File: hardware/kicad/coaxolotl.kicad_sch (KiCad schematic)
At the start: 0 parts

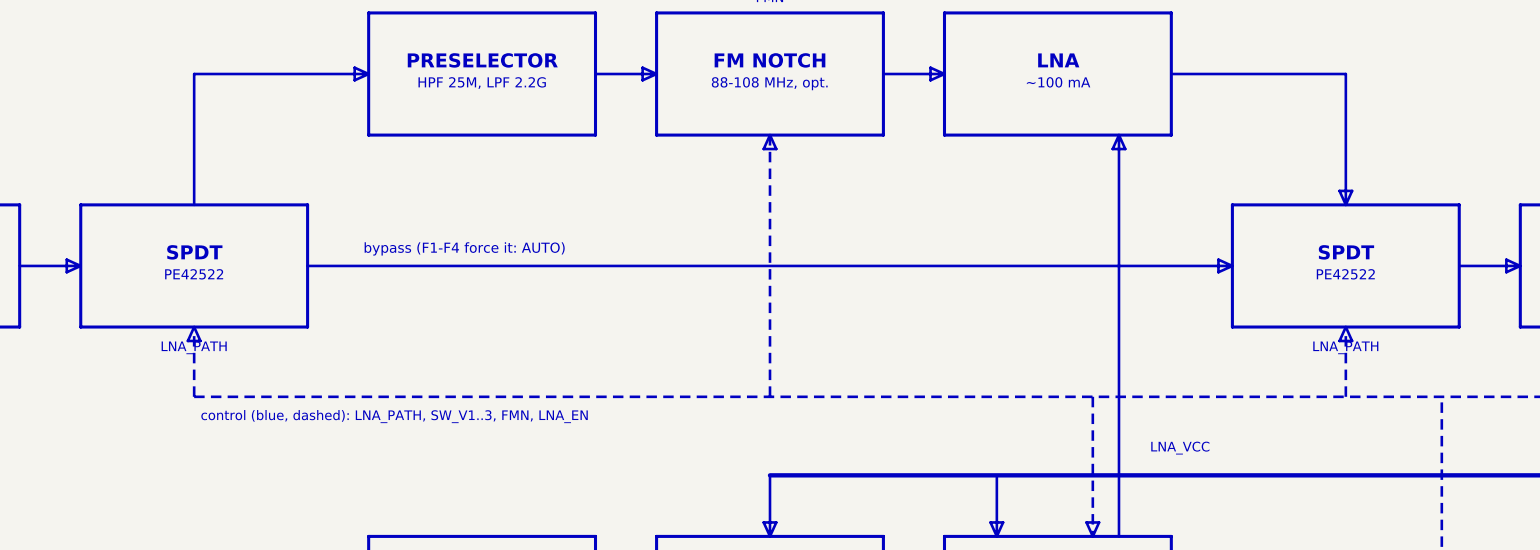
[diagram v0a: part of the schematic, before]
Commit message: Schematic: PE42520 SPDTs instead of PE42522
PE42520C-Z (QFN-16 3x3, LCSC C500478) pinout and truth table checked
against the LCSC datasheet: LS tied to VDD so CTRL = 0 selects RF1
(bypass) and the firmware stays unchanged. KiCad library footprint
QFN-16-1EP_3x3mm_P0.5mm_EP1.7x1.7mm.

Co-Authored-By: Claude Opus 5.5 <noreply@anthropic.com>
Claude-Session: https://claude.ai/code/session_01YRUiF8Vp4242sya9Xyg3TV
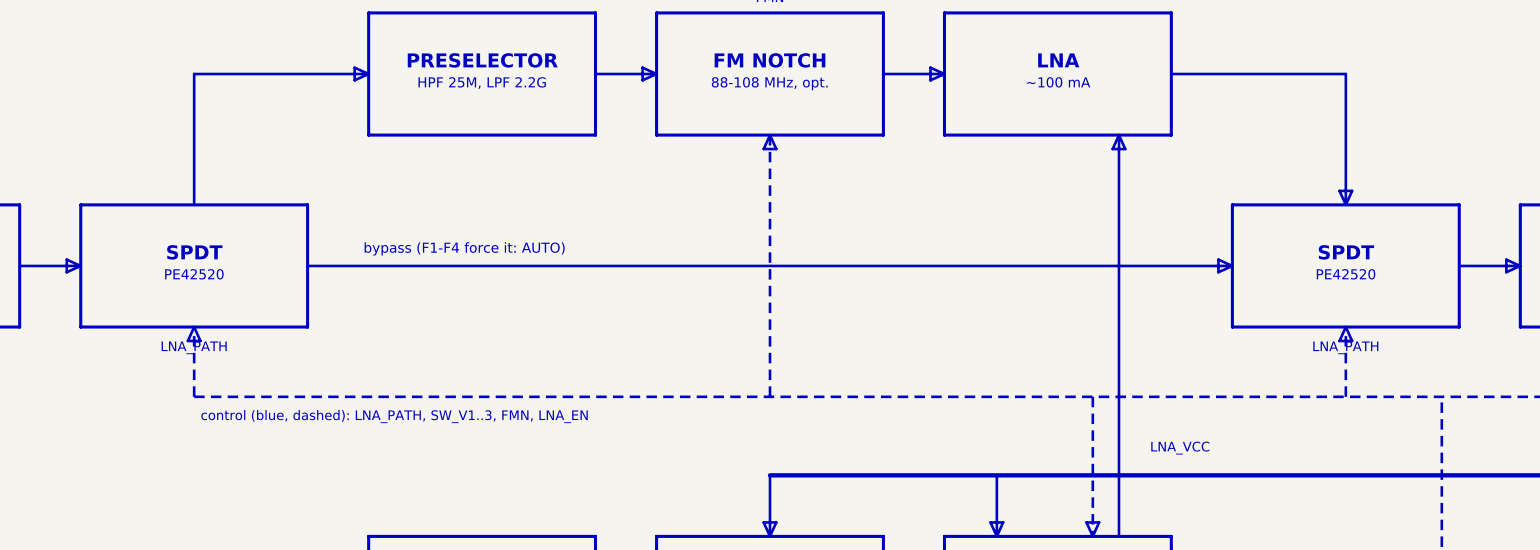
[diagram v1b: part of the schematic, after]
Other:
- note added: "PE42520"
- note removed: "PE42522"
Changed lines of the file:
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@@
     )
   )
-  (text "PE42522"
+  (text "PE42520"
     (at 97 68.25 0)
     (effects
@@
     )
   )
-  (text "PE42522"
+  (text "PE42520"
     (at 229 68.25 0)
     (effects
@@
     (instances
       (project "coaxolotl"
-        (path "/aac636a4-9bcf-4dd9-bf59-957fc0b2357f"
+        (path "/1b55bade-2730-4b67-9af5-55f72c383bca"
           (page "2")
         )
@@
     (instances
       (project "coaxolotl"
-        (path "/aac636a4-9bcf-4dd9-bf59-957fc0b2357f"
+        (path "/1b55bade-2730-4b67-9af5-55f72c383bca"
           (page "3")
         )
@@
     (instances
       (project "coaxolotl"
-        (path "/aac636a4-9bcf-4dd9-bf59-957fc0b2357f"
+        (path "/1b55bade-2730-4b67-9af5-55f72c383bca"
           (page "4")
         )
@@
     (instances
       (project "coaxolotl"
-        (path "/aac636a4-9bcf-4dd9-bf59-957fc0b2357f"
+        (path "/1b55bade-2730-4b67-9af5-55f72c383bca"
           (page "5")
         )
@@
     (instances
       (project "coaxolotl"
-        (path "/aac636a4-9bcf-4dd9-bf59-957fc0b2357f"
+        (path "/1b55bade-2730-4b67-9af5-55f72c383bca"
           (page "6")
         )

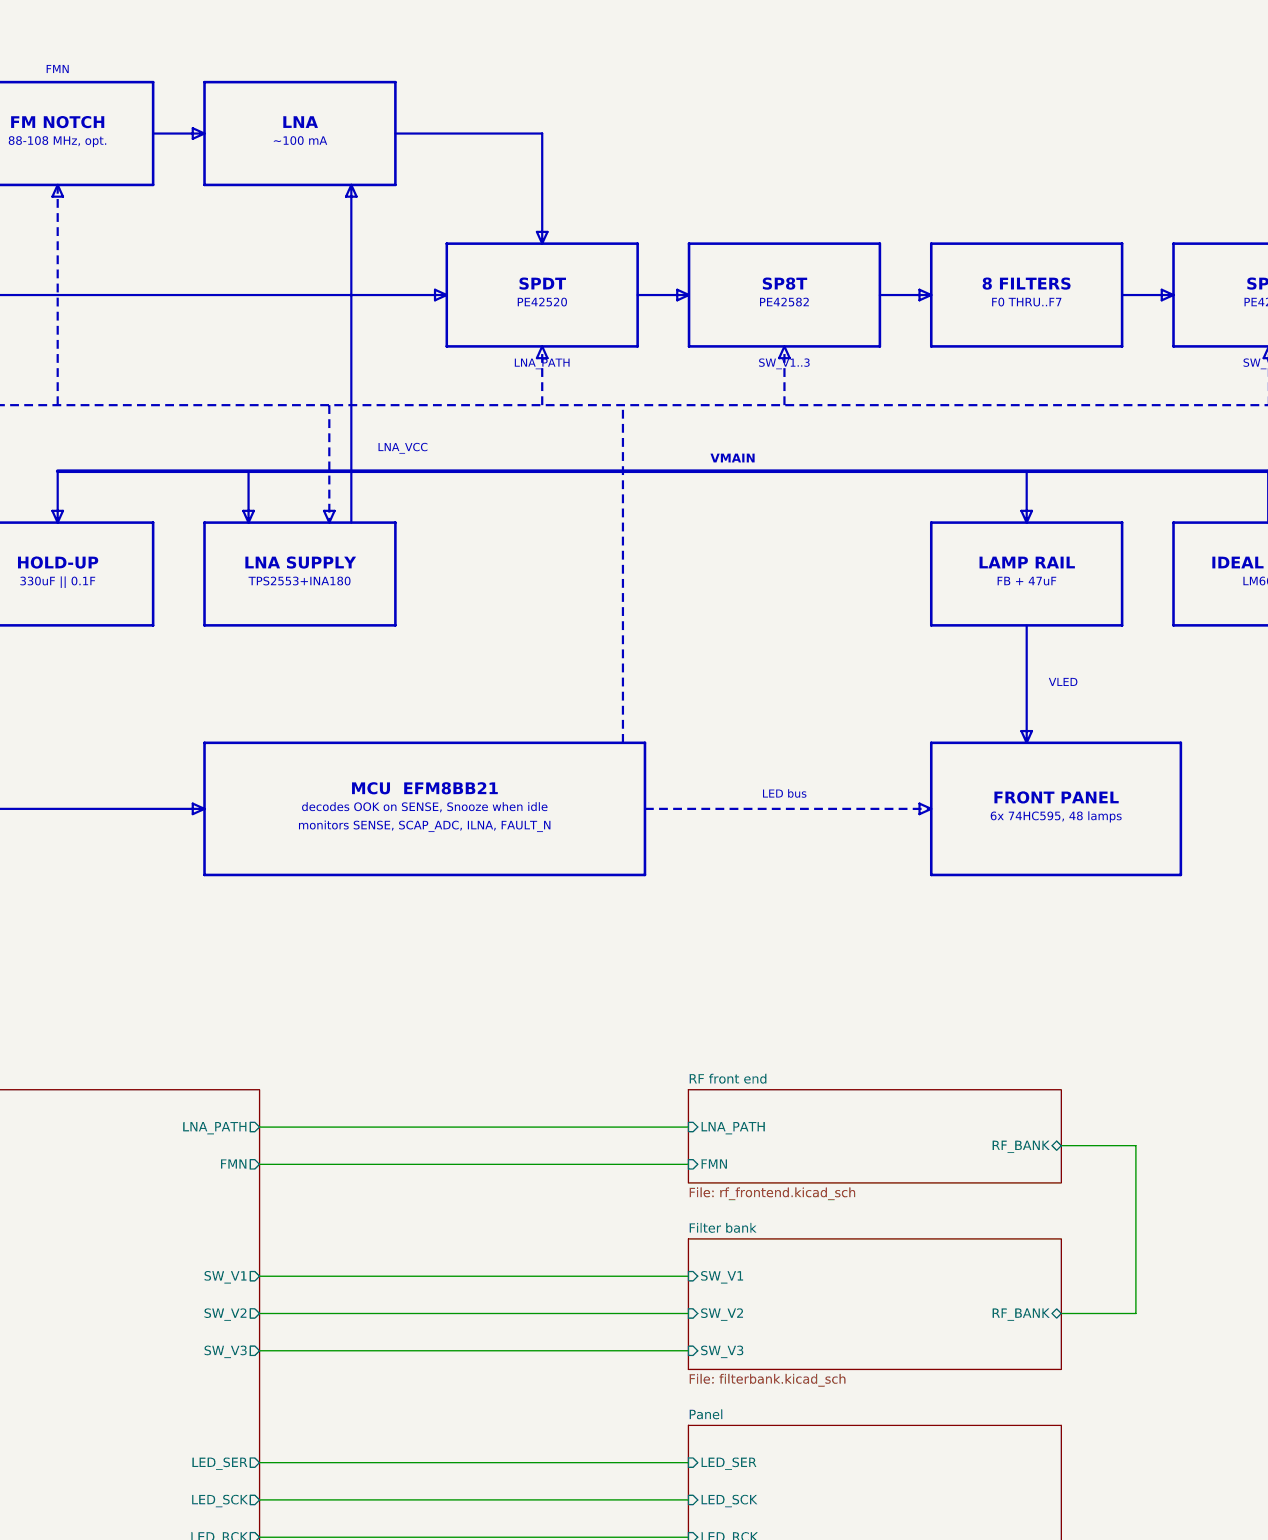
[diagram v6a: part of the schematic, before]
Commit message: U7 on its own GPIO (P1.4 LNA_PATH_OUT)
The output SPDT gets its own control line (same polarity, 10k pull-down),
so the two switches can also be set independently later (e.g. LNA in
circuit on one side only for tests). Firmware drives both together;
179/179 host checks pass.

Co-Authored-By: Claude Opus 5.5 <noreply@anthropic.com>
Claude-Session: https://claude.ai/code/session_01YRUiF8Vp4242sya9Xyg3TV
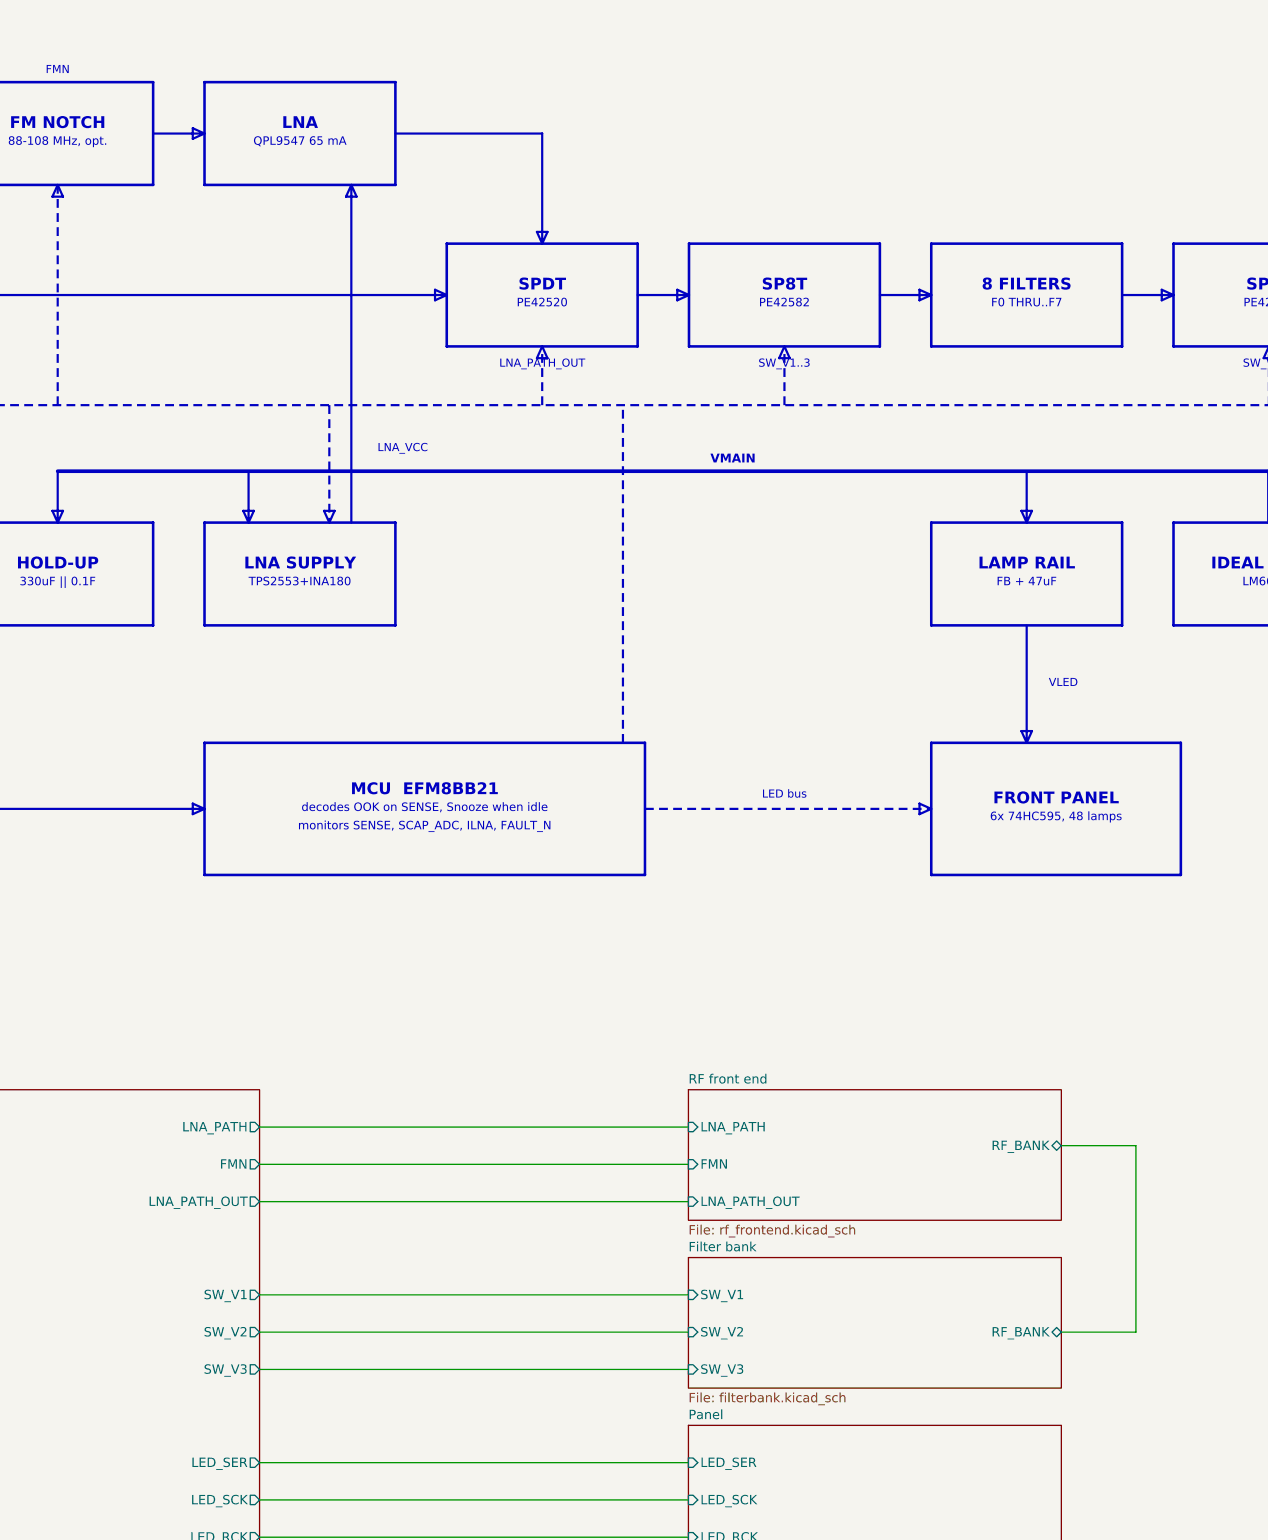
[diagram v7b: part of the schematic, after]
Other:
- sheet MCU ports: added LNA_PATH_OUT; removed none
- sheet RF front end ports: added LNA_PATH_OUT; removed none
- note added: "LNA_PATH_OUT"
- note added: "QPL9547 65 mA"
- note removed: "~100 mA"
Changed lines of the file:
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@@
     )
   )
-  (text "~100 mA"
+  (text "QPL9547 65 mA"
     (at 196 46.25 0)
     (effects
@@
     )
   )
-  (text "LNA_PATH"
+  (text "LNA_PATH_OUT"
     (at 229 76.5 0)
     (effects
@@
   (wire
     (pts
-      (xy 190.5 200.66)
-      (xy 248.92 200.66)
+      (xy 190.5 190.5)
+      (xy 248.92 190.5)
     )
     (stroke
@@
   (wire
     (pts
-      (xy 190.5 205.74)
-      (xy 248.92 205.74)
+      (xy 190.5 203.2)
+      (xy 248.92 203.2)
     )
     (stroke
@@
   (wire
     (pts
-      (xy 190.5 210.82)
-      (xy 248.92 210.82)
+      (xy 190.5 208.28)
+      (xy 248.92 208.28)
     )
     (stroke
@@
   (wire
     (pts
+      (xy 190.5 213.36)
+      (xy 248.92 213.36)
+    )
+    (stroke
+      (width 0)
+      (type default)
+    )
+  )
+  (wire
+    (pts
       (xy 190.5 226.06)
       (xy 248.92 226.06)
@@
     (pts
       (xy 309.88 182.88)
-      (xy 309.88 205.74)
+      (xy 309.88 208.28)
     )
     (stroke
@@
   (wire
     (pts
-      (xy 299.72 205.74)
-      (xy 309.88 205.74)
+      (xy 299.72 208.28)
+      (xy 309.88 208.28)
     )
     (stroke
@@
     (instances
       (project "coaxolotl"
-        (path "/67534585-e0b7-41de-be56-14f8de14b6b9"
+        (path "/bb493d16-8963-485a-b4d1-cc07b45b8f8e"
           (page "2")
         )
@@
       )
     )
+    (pin "LNA_PATH_OUT" output
+      (at 190.5 190.5 0)
+      (effects
+        (font
+          (face "Arial")
+          (size 1.27 1.27)
+        )
+        (justify right)
+      )
+    )
     (pin "SW_V1" output
-      (at 190.5 200.66 0)
+      (at 190.5 203.2 0)
       (effects
         (font
@@
     )
     (pin "SW_V2" output
-      (at 190.5 205.74 0)
+      (at 190.5 208.28 0)
       (effects
         (font
@@
     )
     (pin "SW_V3" output
-      (at 190.5 210.82 0)
+      (at 190.5 213.36 0)
       (effects
         (font
@@
     (instances
       (project "coaxolotl"
-        (path "/67534585-e0b7-41de-be56-14f8de14b6b9"
+        (path "/bb493d16-8963-485a-b4d1-cc07b45b8f8e"
           (page "3")
         )
@@
   (sheet
     (at 248.92 175.26)
-    (size 50.8 12.7)
+    (size 50.8 17.78)
     (fields_autoplaced)
     (stroke
@@
     )
     (property "Sheetfile" "rf_frontend.kicad_sch"
-      (at 248.92 188.56 0)
+      (at 248.92 193.64 0)
       (effects
         (font
@@
       )
     )
+    (pin "LNA_PATH_OUT" input
+      (at 248.92 190.5 180)
+      (effects
+        (font
+          (face "Arial")
+          (size 1.27 1.27)
+        )
+        (justify left)
+      )
+    )
     (pin "RF_BANK" bidirectional
       (at 299.72 182.88 0)
@@
     (instances
       (project "coaxolotl"
-        (path "/67534585-e0b7-41de-be56-14f8de14b6b9"
+        (path "/bb493d16-8963-485a-b4d1-cc07b45b8f8e"
           (page "4")
         )
@@
   )
   (sheet
-    (at 248.92 195.58)
+    (at 248.92 198.12)
     (size 50.8 17.78)
     (fields_autoplaced)
@@
     )
     (property "Sheetname" "Filter bank"
-      (at 248.92 194.88 0)
+      (at 248.92 197.42 0)
       (effects
         (font
@@
     )
     (property "Sheetfile" "filterbank.kicad_sch"
-      (at 248.92 213.96 0)
+      (at 248.92 216.5 0)
       (effects
         (font
@@
     )
     (pin "SW_V1" input
-      (at 248.92 200.66 180)
+      (at 248.92 203.2 180)
       (effects
         (font
@@
     )
     (pin "SW_V2" input
-      (at 248.92 205.74 180)
+      (at 248.92 208.28 180)
       (effects
         (font
@@
     )
     (pin "SW_V3" input
-      (at 248.92 210.82 180)
+      (at 248.92 213.36 180)
       (effects
         (font
@@
     )
     (pin "RF_BANK" bidirectional
-      (at 299.72 205.74 0)
+      (at 299.72 208.28 0)
       (effects
         (font
@@
     (instances
       (project "coaxolotl"
-        (path "/67534585-e0b7-41de-be56-14f8de14b6b9"
+        (path "/bb493d16-8963-485a-b4d1-cc07b45b8f8e"
           (page "5")
         )
@@
     (instances
       (project "coaxolotl"
-        (path "/67534585-e0b7-41de-be56-14f8de14b6b9"
+        (path "/bb493d16-8963-485a-b4d1-cc07b45b8f8e"
           (page "6")
         )
